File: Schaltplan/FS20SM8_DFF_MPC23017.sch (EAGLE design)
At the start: 64 parts, among them IC1 MCP23017SP, IC2 MCP23017SP, IC3 LT1076CT, IC7 MCP23017SP, IC8 MCP23017SP, X10 2092-1153, X11 2092-1153, X12 2092-1152, X3 2092-1152, X4 2092-1153, X5 2092-1153, X6 2092-1153, X7 2092-1153, X8 2092-1153, X9 2092-1153

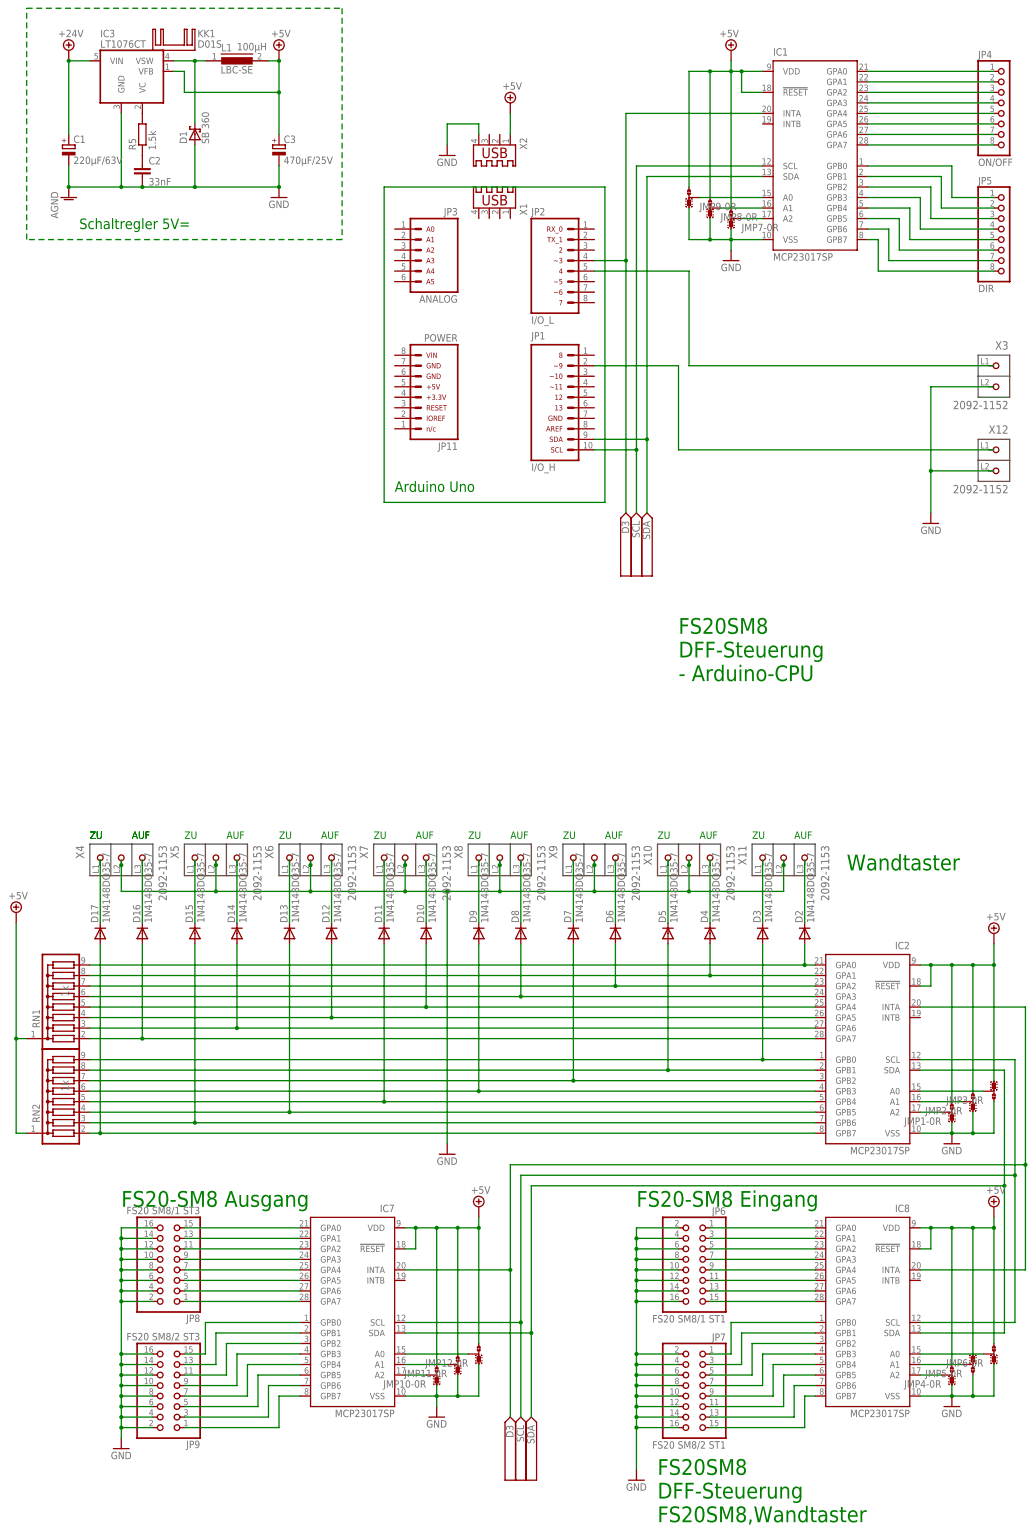
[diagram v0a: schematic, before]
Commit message: Code optimized Circuit small changes
Der Sketch verwendet 29.826 Bytes (92%) des Programmspeicherplatzes. Das Maximum sind 32.256 Bytes.
Globale Variablen verwenden 1.342 Bytes (65%) des dynamischen Speichers, 706 Bytes für lokale Variablen verbleiben. Das Maximum sind 2.048 Bytes.
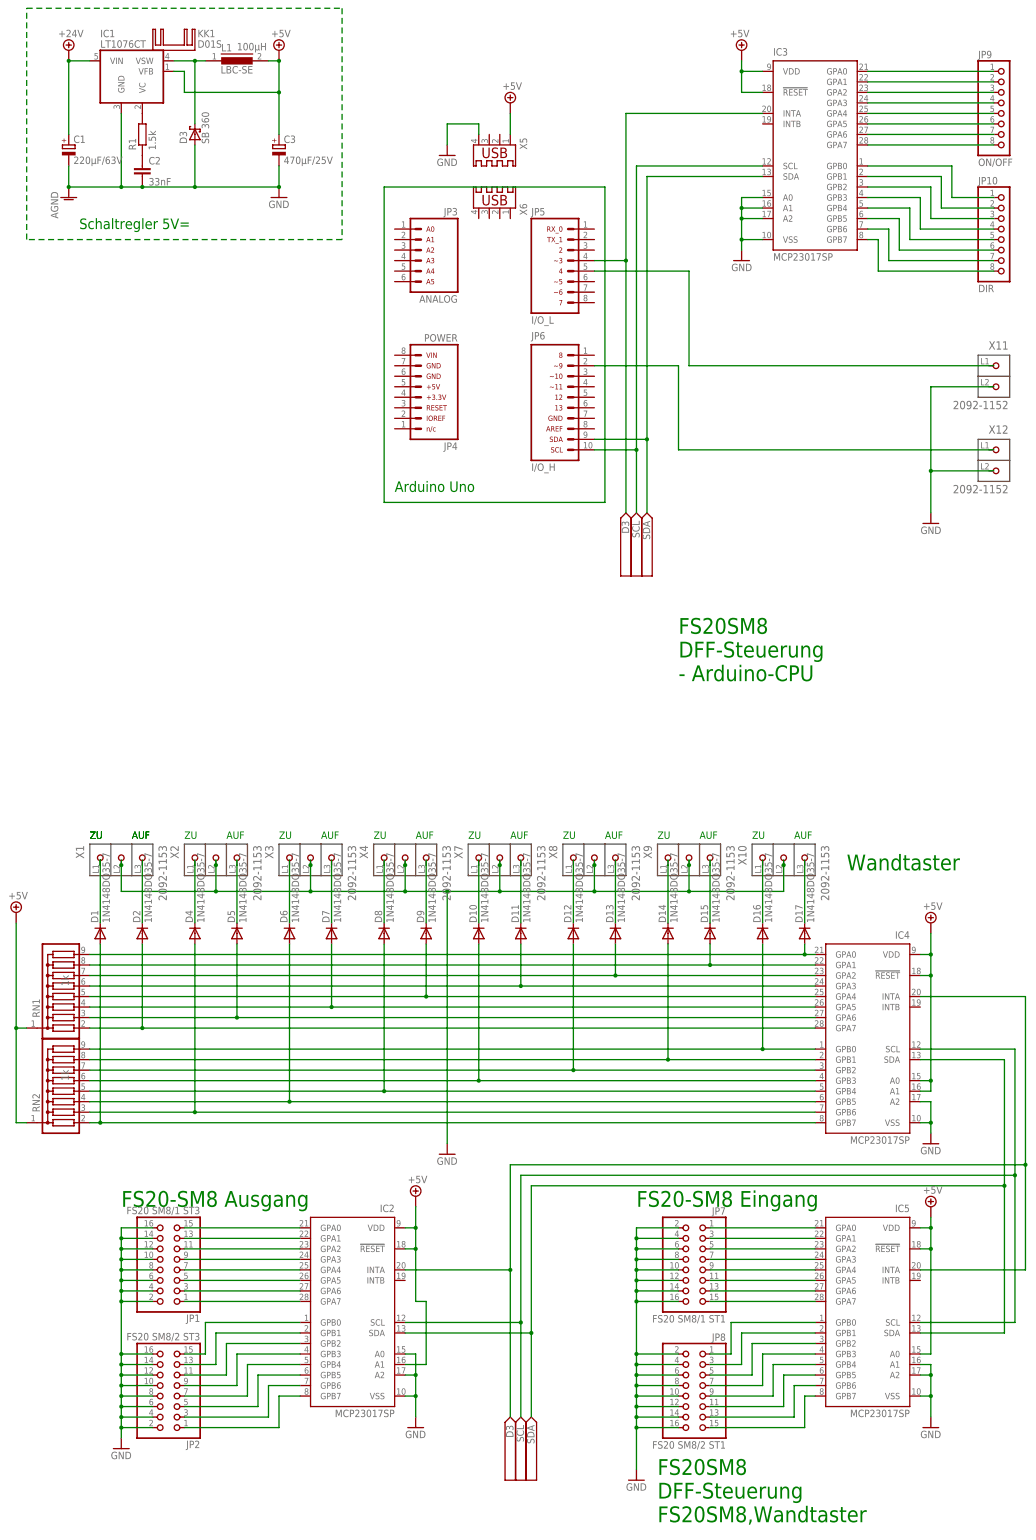
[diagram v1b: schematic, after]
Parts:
- removed IC7: MCP23017SP, microchip:MCP23017SP
- removed JMP1, JMP10, JMP11, JMP12, JMP2, JMP3, JMP4, JMP5, JMP6, JMP7, JMP8, JMP9: 0R-JUMPC, jump-0r-smd:0R-JUMPC
- removed JP11: (no value), arduino_jw:ARDUINO_CONN-POWERSIP
- added IC4: MCP23017SP, microchip:MCP23017SP
- added JP10: DIR, pinhead:PINHD-1X8
- D1: value SB 360 -> 1N4148DO35-7; device diode:SCHOTTKY-DIODEDO201T15 -> diode:1N4148DO35-7
- D3: value 1N4148DO35-7 -> SB 360; device diode:1N4148DO35-7 -> diode:SCHOTTKY-DIODEDO201T15
- IC1: value MCP23017SP -> LT1076CT; device microchip:MCP23017SP -> linear-technology-2:LT1076CT
- IC3: value LT1076CT -> MCP23017SP; device linear-technology-2:LT1076CT -> microchip:MCP23017SP
- JP1: value ARDUINO_CONN-IO_HSIP -> FS20 SM8/1 ST3; device arduino_jw:ARDUINO_CONN-IO_HSIP -> pinhead:PINHD-2X8
- JP2: value (none) -> FS20 SM8/2 ST3; device arduino_jw:ARDUINO_CONN-IO_LSIP -> pinhead:PINHD-2X8
- JP4: value ON/OFF -> (none); device pinhead:PINHD-1X8 -> arduino_jw:ARDUINO_CONN-POWERSIP
- JP5: value DIR -> (none); device pinhead:PINHD-1X8 -> arduino_jw:ARDUINO_CONN-IO_LSIP
- JP6: value FS20 SM8/1 ST1 -> ARDUINO_CONN-IO_HSIP; device pinhead:PINHD-2X8 -> arduino_jw:ARDUINO_CONN-IO_HSIP
- JP7: value FS20 SM8/2 ST1 -> FS20 SM8/1 ST1
- JP8: value FS20 SM8/1 ST3 -> FS20 SM8/2 ST1
- JP9: value FS20 SM8/2 ST3 -> ON/OFF; device pinhead:PINHD-2X8 -> pinhead:PINHD-1X8
- X1, X2: value (none) -> 2092-1153; device con-yamaichi:USB-A003 -> con-wago_5.0mm:2092-1153
- X11: value 2092-1153 -> 2092-1152; device con-wago_5.0mm:2092-1153 -> con-wago_5.0mm:2092-1152
- X3: value 2092-1152 -> 2092-1153; device con-wago_5.0mm:2092-1152 -> con-wago_5.0mm:2092-1153
- X5, X6: value 2092-1153 -> (none); device con-wago_5.0mm:2092-1153 -> con-yamaichi:USB-A003
- renumbered IC8 to IC5, R5 to R1
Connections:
- removed net N$114: IC2.A2, JMP1-0R.2
- removed net N$115: IC2.A0, JMP3-0R.2
- removed net N$116: IC5.A1, JMP5-0R.2
- removed net N$117: IC5.A2, JMP4-0R.2
- removed net N$118: IC5.A0, JMP6-0R.2
- removed net N$137: IC7.A0, JMP12-0R.2
- removed net N$138: IC7.A2, JMP10-0R.2
- removed net N$139: IC7.A1, JMP11-0R.2
- removed net N$58: IC1.A0, JMP9-0R.2
- removed net N$59: IC1.A2, JMP7-0R.2
- removed net N$60: IC1.A1, JMP8-0R.2
- removed net N$98: IC2.A1, JMP2-0R.2
- net +24V: now also IC1.VIN; no longer IC3.VIN
- net +5V: now also IC1.VFB, IC2.A1, IC3.!RESET, IC3.VDD, IC4.!RESET, IC4.A0, IC4.A1, IC4.VDD, IC5.A0, X5.1; no longer IC1.!RESET, IC1.VDD, IC3.VFB, IC7.!RESET, IC7.VDD, JMP1-0R.3, JMP10-0R.3, JMP11-0R.3, JMP12-0R.3, JMP2-0R.3, JMP3-0R.3, JMP4-0R.3, JMP5-0R.3, JMP6-0R.3, JMP7-0R.3, JMP8-0R.3, JMP9-0R.3, X2.1
- net AGND: now also D3.A, IC1.GND; no longer D1.A, IC3.GND
- net GND: now also IC2.A0, IC2.A2, IC3.A0, IC3.A1, IC3.A2, IC3.VSS, IC4.A2, IC4.VSS, IC5.A1, IC5.A2, JP1.10, JP1.12, JP1.14, JP1.16, JP1.2, JP1.4, JP1.6, JP1.8, JP2.10, JP2.12, JP2.14, JP2.16, JP2.2, JP2.4, JP2.6, JP2.8, X1.P2, X2.P2, X3.P2, X5.4; no longer IC1.VSS, IC7.VSS, JMP1-0R.1, JMP10-0R.1, JMP11-0R.1, JMP12-0R.1, JMP2-0R.1, JMP3-0R.1, JMP4-0R.1, JMP5-0R.1, JMP6-0R.1, JMP7-0R.1, JMP8-0R.1, JMP9-0R.1, JP6.10, JP6.12, JP6.14, JP6.16, JP6.2, JP6.4, JP6.6, JP6.8, JP9.10, JP9.12, JP9.14, JP9.16, JP9.2, JP9.4, JP9.6, JP9.8, X11.P2, X2.4, X5.P2, X6.P2
- net N$100: now also D14.A, IC4.GPB1; no longer D5.A, IC2.GPB1
- net N$101: now also D13.A, IC4.GPA2; no longer D6.A, IC2.GPA2
- net N$102: now also D12.A, IC4.GPB2; no longer D7.A, IC2.GPB2
- net N$103: now also D11.A, IC4.GPA3; no longer D8.A, IC2.GPA3
- net N$104: now also D10.A, IC4.GPB3; no longer D9.A, IC2.GPB3
- net N$105: now also D15.A, IC4.GPA1; no longer D4.A, IC2.GPA1
- net N$106: now also D9.A, IC4.GPA4; no longer D10.A, IC2.GPA4
- net N$107: now also D8.A, IC4.GPB4; no longer D11.A, IC2.GPB4
- net N$108: now also D7.A, IC4.GPA5; no longer D12.A, IC2.GPA5
- net N$109: now also D6.A, IC4.GPB5; no longer D13.A, IC2.GPB5
- net N$110: now also D5.A, IC4.GPA6; no longer D14.A, IC2.GPA6
- net N$111: now also D4.A, IC4.GPB6; no longer D15.A, IC2.GPB6
- net N$112: now also D2.A, IC4.GPA7; no longer D16.A, IC2.GPA7
- net N$113: now also D1.A, IC4.GPB7; no longer D17.A, IC2.GPB7
- net N$12: now also IC3.GPB0, JP10.1; no longer IC1.GPB0, JP5.1
- net N$123: now also IC2.GPB0, JP2.15; no longer IC7.GPB0, JP9.15
- net N$127: now also IC2.GPB1, JP2.13; no longer IC7.GPB1, JP9.13
- net N$128: now also IC2.GPB2, JP2.11; no longer IC7.GPB2, JP9.11
- net N$129: now also IC2.GPB3, JP2.9; no longer IC7.GPB3, JP9.9
- net N$13: now also IC3.GPB1, JP10.2; no longer IC1.GPB1, JP5.2
- net N$130: now also IC2.GPB4, JP2.7; no longer IC7.GPB4, JP9.7
- net N$131: now also IC2.GPB5, JP2.5; no longer IC7.GPB5, JP9.5
- net N$132: now also IC2.GPB6, JP2.3; no longer IC7.GPB6, JP9.3
- net N$133: now also IC2.GPB7, JP2.1; no longer IC7.GPB7, JP9.1
- net N$14: now also IC3.GPB2, JP10.3; no longer IC1.GPB2, JP5.3
- net N$15: now also IC3.GPB3, JP10.4; no longer IC1.GPB3, JP5.4
- net N$16: now also IC1.VC; no longer IC3.VC
- net N$17: now also IC3.GPB4, JP10.5; no longer IC1.GPB4, JP5.5
- net N$18: now also IC3.GPB5, JP10.6; no longer IC1.GPB5, JP5.6
- net N$19: now also IC2.GPA0, JP1.15; no longer IC7.GPA0, JP8.15
- net N$2: now also JP5.5; no longer JP2.5
- net N$20: now also IC3.GPB6, JP10.7; no longer IC1.GPB6, JP5.7
- net N$21: now also D1.C, X1.P1; no longer D17.C, X4.P1
- net N$22: now also D2.C, X1.P3; no longer D16.C, X4.P3
- net N$23: now also D5.C, X2.P3; no longer D14.C, X5.P3
- net N$24: now also D4.C, X2.P1; no longer D15.C, X5.P1
- net N$25: now also D7.C, X3.P3; no longer D12.C, X6.P3
- net N$26: now also D6.C, X3.P1; no longer D13.C, X6.P1
- net N$27: now also D8.C, X4.P1; no longer D11.C, X7.P1
- net N$28: now also IC3.GPA0, JP9.1; no longer IC1.GPA0, JP4.1
- net N$29: now also IC3.GPA1, JP9.2; no longer IC1.GPA1, JP4.2
- net N$3: now also IC3.INTA, JP5.4; no longer IC1.INTA, JP2.4
- net N$30: now also IC3.GPA2, JP9.3; no longer IC1.GPA2, JP4.3
- net N$31: now also IC3.GPA3, JP9.4; no longer IC1.GPA3, JP4.4
- net N$32: now also D9.C, X4.P3; no longer D10.C, X7.P3
- net N$33: now also D10.C, X7.P1; no longer D9.C, X8.P1
- net N$34: now also D11.C, X7.P3; no longer D8.C, X8.P3
- net N$35: now also D12.C, X8.P1; no longer D7.C, X9.P1
- net N$36: now also IC3.GPA4, JP9.5; no longer IC1.GPA4, JP4.5
- net N$37: now also IC3.GPA5, JP9.6; no longer IC1.GPA5, JP4.6
- net N$38: now also IC3.GPA6, JP9.7; no longer IC1.GPA6, JP4.7
- net N$39: now also IC3.GPA7, JP9.8; no longer IC1.GPA7, JP4.8
- net N$4: now also IC3.SCL, JP6.10; no longer IC1.SCL, JP1.10
- net N$48: now also D13.C, X8.P3; no longer D6.C, X9.P3
- net N$5: now also IC3.SDA, JP6.9; no longer IC1.SDA, JP1.9
- net N$50: now also D14.C, X9.P1; no longer D5.C, X10.P1
- net N$51: now also D15.C, X9.P3; no longer D4.C, X10.P3
- net N$52: now also D16.C, X10.P1; no longer D3.C, X11.P1
- net N$53: now also D17.C, X10.P3; no longer D2.C, X11.P3
- net N$54: now also IC3.GPB7, JP10.8; no longer IC1.GPB7, JP5.8
- net N$55: now also JP8.1; no longer JP7.1
- net N$56: now also JP8.3; no longer JP7.3
- net N$57: now also JP8.5; no longer JP7.5
- net N$6: now also JP6.2; no longer JP1.2
- net N$61: now also IC2.GPA1, JP1.13; no longer IC7.GPA1, JP8.13
- net N$62: now also IC2.GPA2, JP1.11; no longer IC7.GPA2, JP8.11
- net N$63: now also D3.C, IC1.VSW; no longer D1.C, IC3.VSW
- net N$67: now also IC2.GPA3, JP1.9; no longer IC7.GPA3, JP8.9
- net N$68: now also IC2.GPA4, JP1.7; no longer IC7.GPA4, JP8.7
- net N$71: now also IC2.GPA5, JP1.5; no longer IC7.GPA5, JP8.5
- net N$73: now also IC2.GPA6, JP1.3; no longer IC7.GPA6, JP8.3
- net N$74: now also IC2.GPA7, JP1.1; no longer IC7.GPA7, JP8.1
- net N$75: now also JP7.1; no longer JP6.1
- net N$76: now also JP7.3; no longer JP6.3
- net N$77: now also JP7.5; no longer JP6.5
- net N$78: now also JP7.7; no longer JP6.7
- net N$79: now also JP7.9; no longer JP6.9
- net N$80: now also JP7.11; no longer JP6.11
- net N$83: now also JP7.13; no longer JP6.13
- net N$84: now also JP7.15; no longer JP6.15
- net N$85: now also JP8.7; no longer JP7.7
- net N$86: now also JP8.9; no longer JP7.9
- net N$87: now also JP8.11; no longer JP7.11
- net N$88: now also JP8.13; no longer JP7.13
- net N$89: now also JP8.15; no longer JP7.15
- net N$91: now also IC4.SCL; no longer IC7.SCL
- net N$92: now also IC4.SDA; no longer IC7.SDA
- net N$93: now also IC4.INTA; no longer IC7.INTA
- net N$95: now also D17.A, IC4.GPA0; no longer D2.A, IC2.GPA0
- net N$99: now also D16.A, IC4.GPB0; no longer D3.A, IC2.GPB0
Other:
- moved on the sheet: D10, D11, D12, D13, D14, D15, D16, D17, D2, D4, D5, D6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
